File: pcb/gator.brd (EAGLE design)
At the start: 101.6 x 81.3 mm, 81 parts, among them J2 POWER_JACKPTH, X1 USB-A-S, Y1 12MHz

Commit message: any recent changes before break
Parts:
- moved C9 34.9 mm to (90.2, 41.9), turned to 0 degrees
- moved D1 18.5 mm to (76.2, 72.4), turned to 90 degrees
- moved C14 13.3 mm to (96.5, 53.3), turned to 90 degrees
- moved C31 13.0 mm to (86.4, 35.6)
- moved R10 11.7 mm to (82.5, 64.8), turned to 90 degrees
- moved R7 10.9 mm to (90.2, 50.2), turned to 0 degrees
- moved C8 10.8 mm to (81.3, 38.1)
- moved C7 7.73 mm to (86.4, 47.0)
- moved R26 7.67 mm to (59.7, 71.8), turned to 0 degrees
- moved MIC5219-3.3YM5_1 6.35 mm to (90.2, 47.0)
- moved R24 6.35 mm to (71.1, 15.2), turned to 270 degrees
- moved R9 5.08 mm to (87.6, 58.4)
- moved C23 3.81 mm to (77.5, 45.7)
- moved R12 3.81 mm to (81.3, 47.0)
- moved OSC_50M 2.01 mm to (59.1, 67.3), turned to 270 degrees
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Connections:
- net N$10 renamed RD-
- net N$11 renamed TD+
- net N$12 renamed TD-
- net N$9 renamed RD+
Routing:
- net +3V3: track 56.1 -> 126.5 mm, vias 2 -> 3
- net V+: track 0.00 -> 58.7 mm
- net VCCIO: track 206.6 -> 234.4 mm
- net TD-: track 0.00 -> 20.2 mm
- net TD+: track 0.00 -> 19.2 mm
- net RD-: track 0.00 -> 14.6 mm
- net N$3: track 21.0 -> 6.46 mm
- net RD+: track 0.00 -> 12.6 mm
- net NRST: track 45.0 -> 50.2 mm
- net N$7: track 0.00 -> 3.05 mm
- net N$5: track 0.00 -> 1.92 mm
- net SD_DETECT: track 32.2 -> 33.9 mm
- net TDO/SWO: vias 0 -> 1

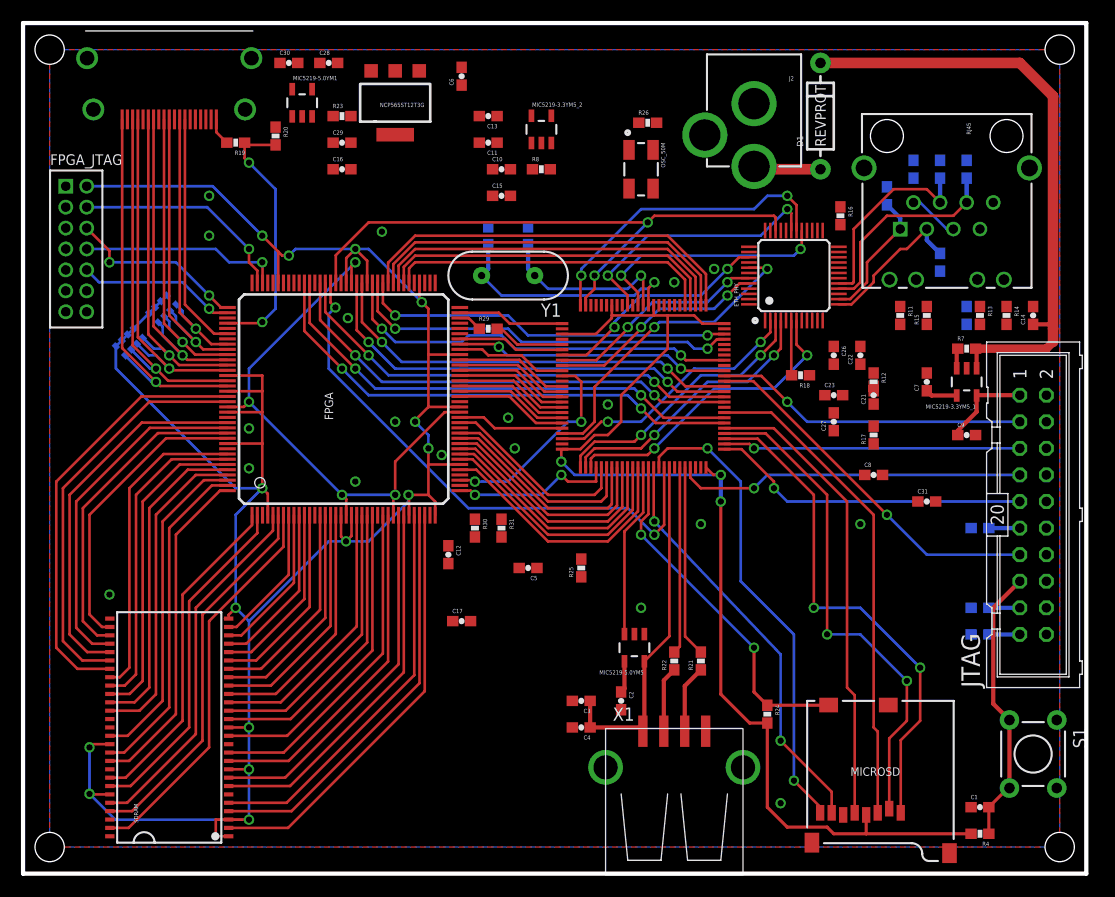
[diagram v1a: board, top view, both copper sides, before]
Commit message: Routed and cleaned up USB power, SD card signals, ethernet phy
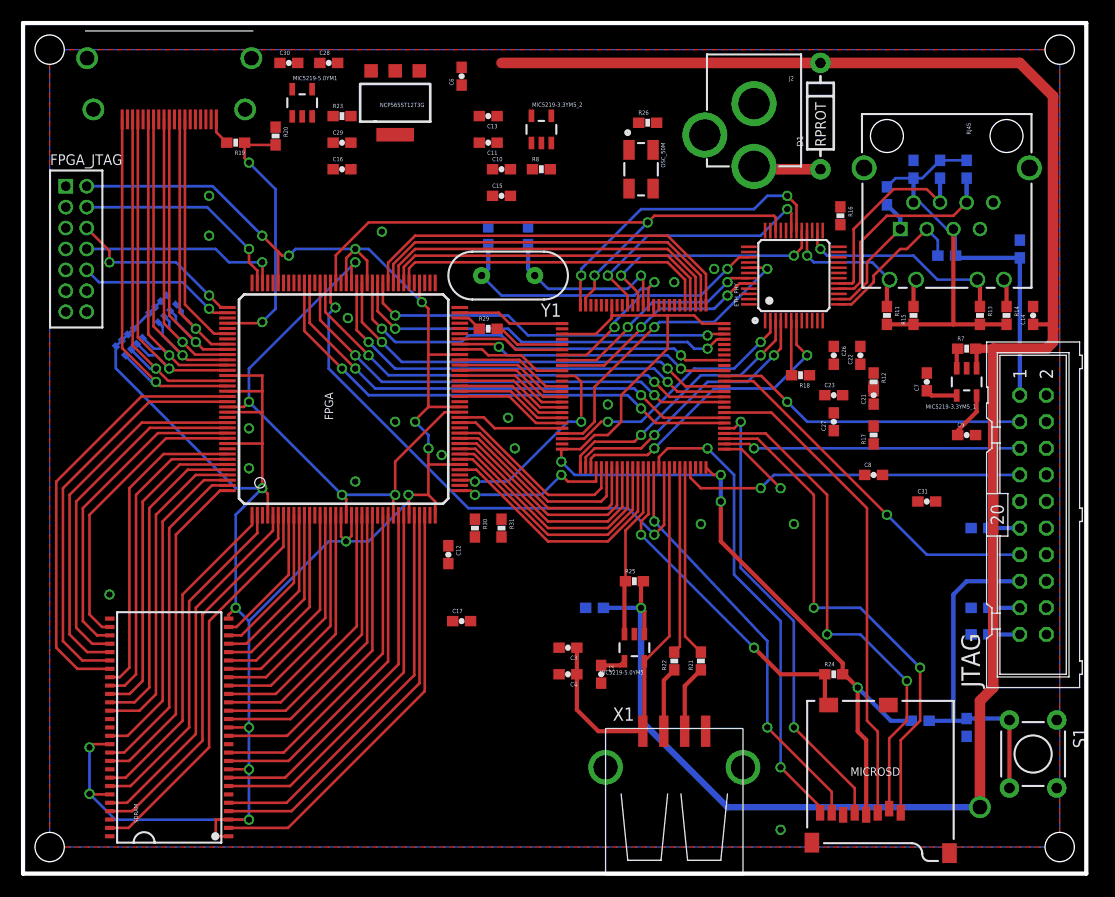
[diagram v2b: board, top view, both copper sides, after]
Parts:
- D1: value REVPROT -> RPROT
- moved R4 12.2 mm to (85.7, 14.6), flipped to the bottom, turned to 0 degrees
- moved C24 8.13 mm to (95.2, 59.7)
- moved C1 7.73 mm to (90.2, 14.0), flipped to the bottom, turned to 90 degrees
- moved C5 7.41 mm to (54.6, 25.4), flipped to the bottom, turned to 0 degrees
- moved R24 7.41 mm to (77.5, 19.1), turned to 0 degrees
- moved C3 5.24 mm to (52.1, 21.6)
- moved C4 5.24 mm to (52.1, 19.1)
- moved R25 5.24 mm to (58.4, 27.9), turned to 0 degrees
- moved C2 3.18 mm to (55.2, 19.1)
- moved R11 1.27 mm to (82.5, 53.3)
- moved R15 1.27 mm to (85.1, 53.3)
- moved R9 0.90 mm to (88.3, 59.1), turned to 180 degrees
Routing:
- net V+: track 58.7 -> 189.0 mm, vias 1 -> 2
- net +3V3: track 126.5 -> 163.8 mm, vias 3 -> 4
- net TCK/SWCLK: track 30.7 -> 6.92 mm
- net LED_ACT: track 0.00 -> 20.8 mm, vias 0 -> 1
- net LED_LINK: track 0.00 -> 13.9 mm, vias 0 -> 1
- net NRST: track 50.2 -> 56.9 mm
- net USB_VBUS: track 34.0 -> 39.3 mm
- net N$14: track 0.00 -> 2.68 mm
- net N$13: track 0.00 -> 2.68 mm
- net SD_CLK: track 44.7 -> 43.7 mm, vias 0 -> 2
- net SD_DETECT: track 33.9 -> 32.9 mm
- net N$4: track 3.06 -> 2.39 mm

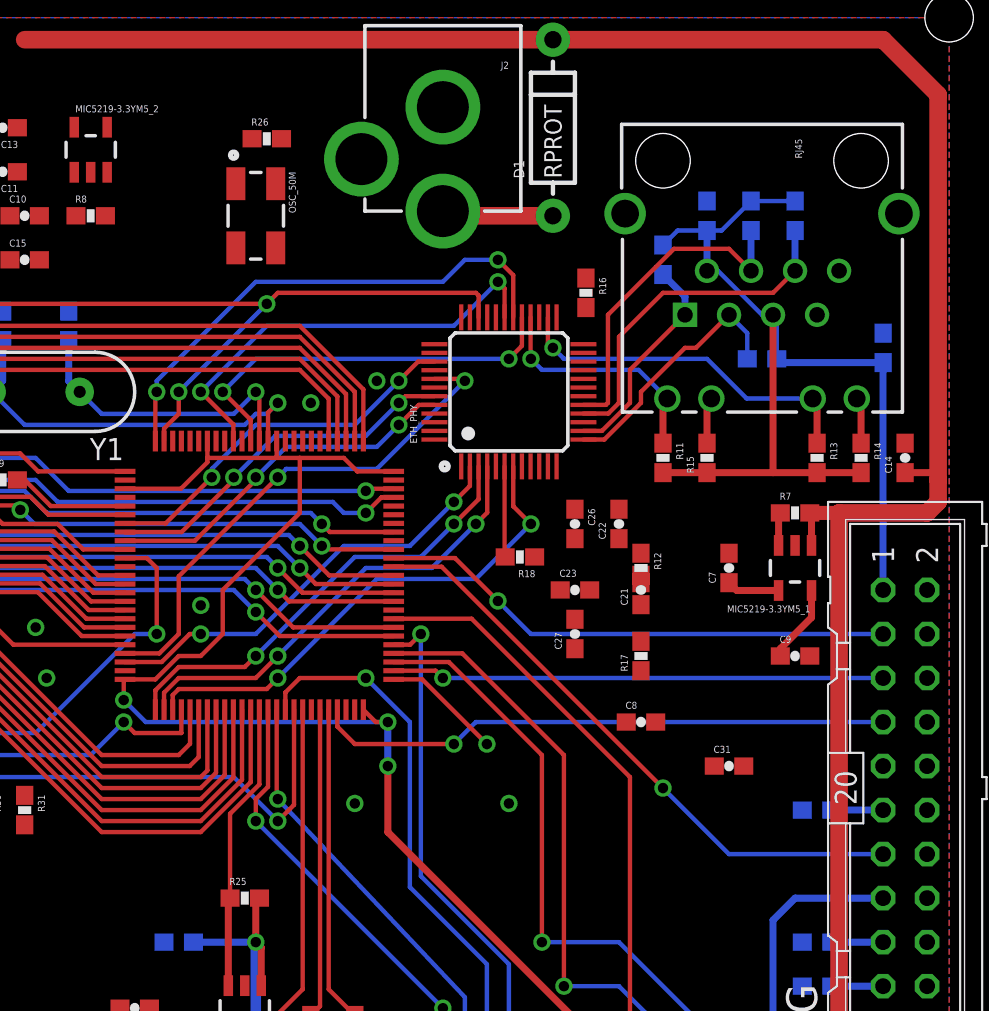
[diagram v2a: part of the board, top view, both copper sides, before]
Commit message: Finished routing ethernet
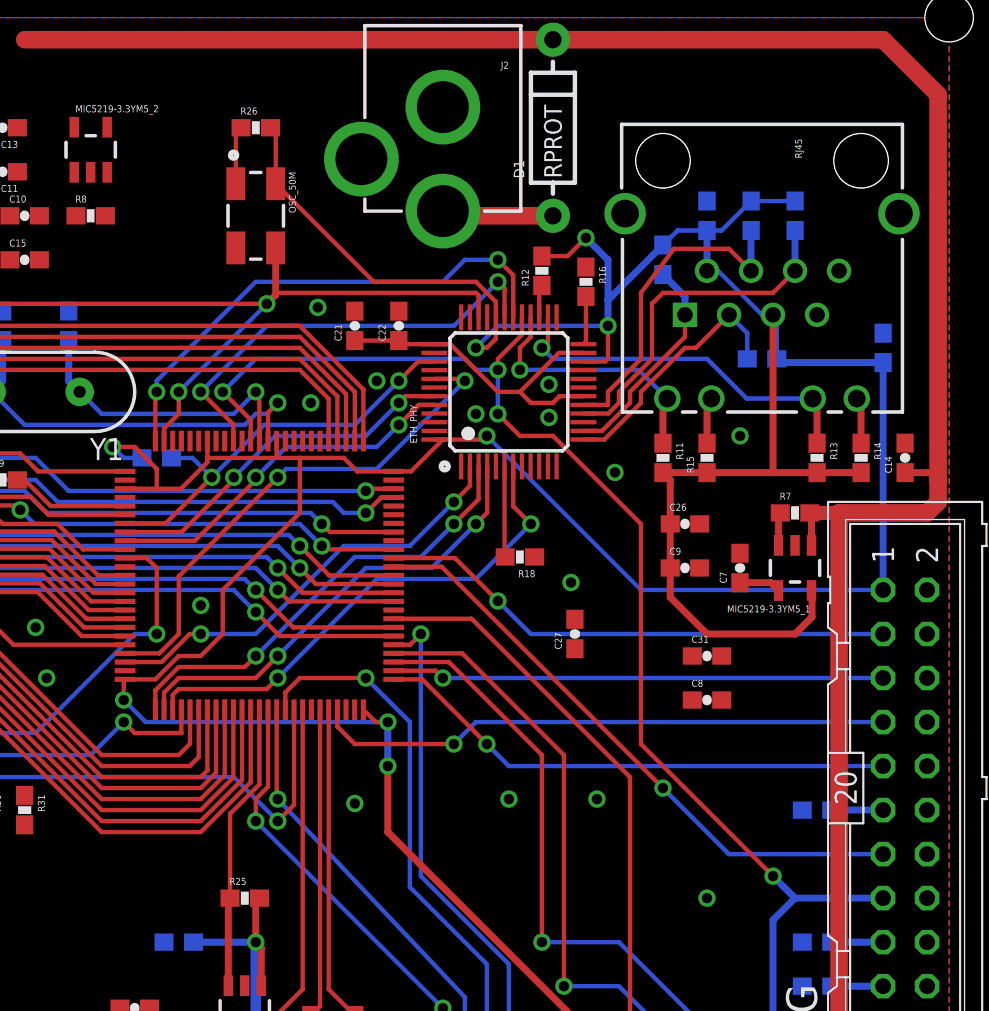
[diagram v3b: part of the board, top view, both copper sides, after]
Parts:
- removed C23: 100n, SparkFun-Passives:0603-CAP
- moved R17 30.2 mm to (53.3, 53.3), flipped to the bottom, turned to 0 degrees
- moved C21 22.5 mm to (64.8, 61.0)
- moved R12 18.1 mm to (75.6, 64.1), turned to 90 degrees
- moved C22 17.1 mm to (67.3, 61.0)
- moved C9 8.13 mm to (83.8, 47.0)
- moved C31 6.48 mm to (85.1, 41.9)
- moved C26 6.35 mm to (83.8, 49.5), turned to 0 degrees
- moved C8 4.02 mm to (85.1, 39.4)
- moved R26 0.90 mm to (59.1, 72.4)
- moved C7 0.64 mm to (87.0, 47.0)
- moved R16 0.63 mm to (78.1, 63.5)
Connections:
- net GND: no longer C23.2
- net PFB: no longer C23.1
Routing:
- net +3V3: track 163.8 -> 264.1 mm, vias 4 -> 9
- net NRST: track 56.9 -> 96.1 mm, vias 2 -> 4
- net TCK/SWCLK: track 6.92 -> 30.3 mm
- net PFB: track 0.00 -> 19.6 mm
- net 50MHZ_OSC: track 57.9 -> 61.4 mm
- net N$31: track 0.00 -> 3.35 mm
- net N$16: track 0.00 -> 2.81 mm
- net RMII_CRSDV: track 22.0 -> 24.5 mm
- net N$17: track 0.00 -> 1.90 mm
- net LED_LINK: track 13.9 -> 15.2 mm
- net LED_ACT: track 20.8 -> 21.4 mm
- net N$7: track 3.05 -> 2.41 mm

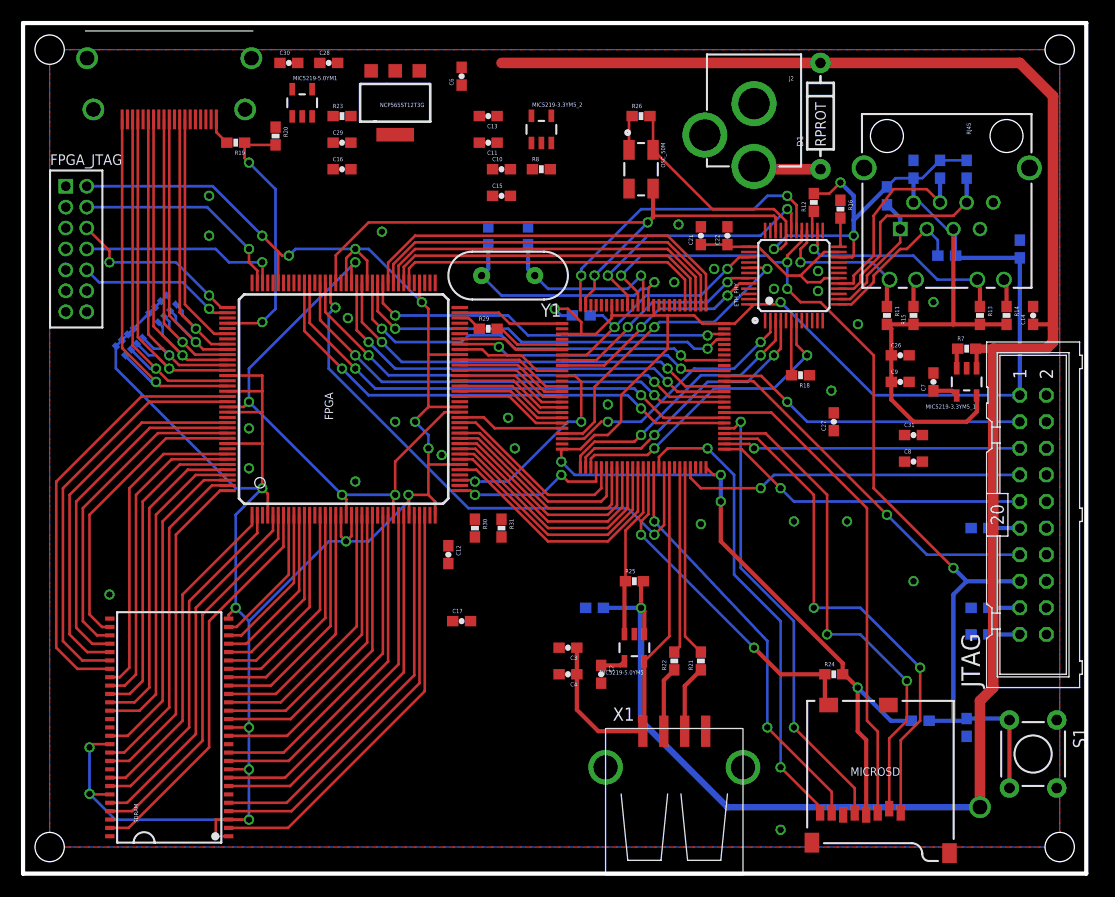
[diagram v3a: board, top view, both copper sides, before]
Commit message: Finished routing CEC, DDC, and remaining power; still have to do decoupling caps
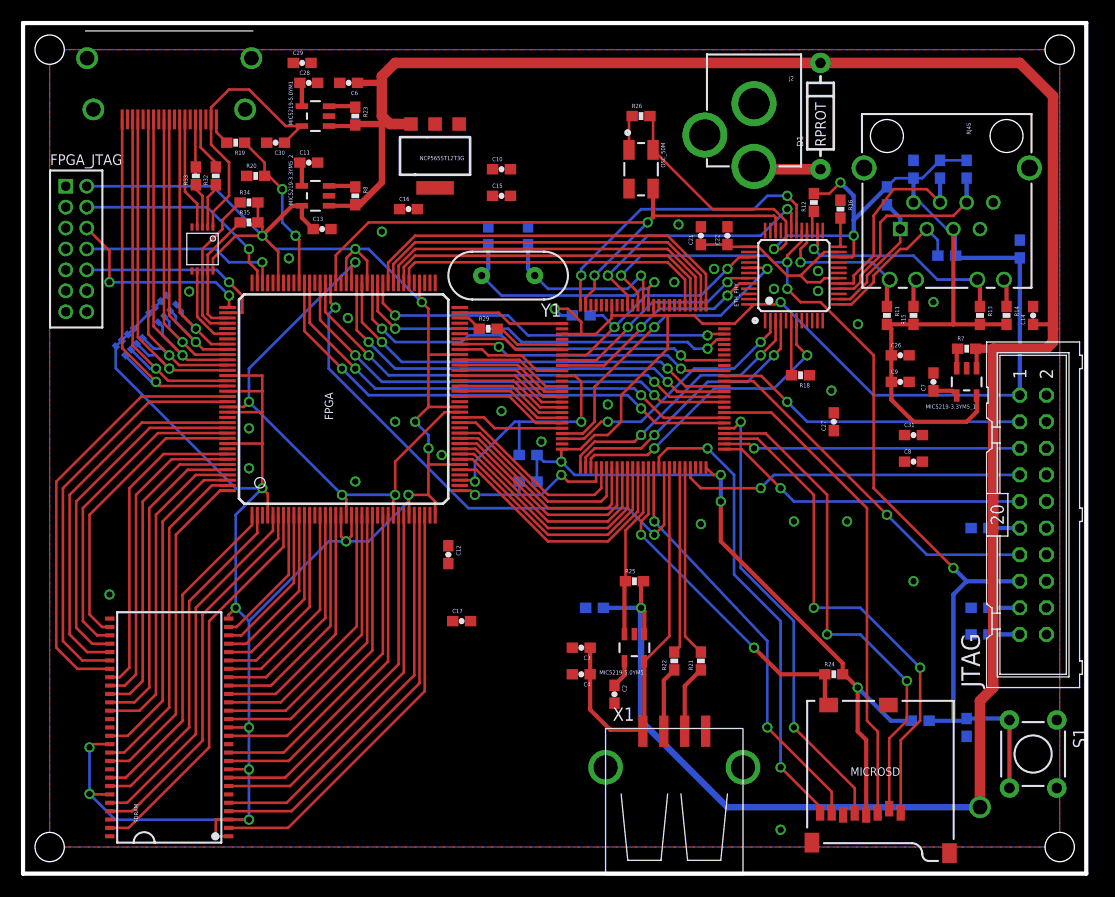
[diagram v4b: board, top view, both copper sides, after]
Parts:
- added R32, R33: 22, SparkFun-Passives:0603-RES
- added R34, R35: 10K, SparkFun-Passives:0603-RES
- added U$3: PCA9527, gator:TSSOP10
- moved MIC5219-3.3YM5_2 22.5 mm to (27.9, 64.8), turned to 90 degrees
- moved C13 19.2 mm to (28.6, 61.6), turned to 0 degrees
- moved R8 18.0 mm to (31.8, 64.8), turned to 270 degrees
- moved C11 17.3 mm to (27.3, 67.9), turned to 0 degrees
- moved C6 10.8 mm to (31.1, 75.6), turned to 180 degrees
- moved C29 8.52 mm to (26.7, 77.5)
- moved C30 7.73 mm to (24.1, 69.8), turned to 180 degrees
- moved R31 7.43 mm to (48.3, 40.0), flipped to the bottom, turned to 180 degrees
- moved C16 7.41 mm to (36.8, 63.5)
- moved R30 6.75 mm to (48.3, 37.5), flipped to the bottom, turned to 180 degrees
- moved NCP565ST12T3G 6.35 mm to (39.4, 68.6)
- moved R20 4.26 mm to (22.2, 66.7), turned to 0 degrees
- moved C28 2.69 mm to (27.3, 75.6)
- moved C2 2.29 mm to (56.5, 17.1)
- moved MIC5219-5.0YM1 1.80 mm to (27.9, 72.4), turned to 90 degrees
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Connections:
- new net CEC_INT: FPGA.P114, U$3.7
- new net DDCC_INT: FPGA.P112, R34.1, U$3.8
- new net DDCD_INT: FPGA.P111, R35.1, U$3.9
- new net DDC_EN: U$3.6
- new net N$10: R33.1, U$3.3
- new net N$9: R32.1, U$3.2
- net CEC: now also U$3.4; no longer FPGA.P114
- net DDC_CLK: now also R33.2
- net DDC_DATA: now also R32.2
- net GND: now also U$3.5
- net HDMI_5V: now also U$3.1
- net HDMI_DETECT: now also FPGA.P99; no longer FPGA.P112
- net VCCIO: now also R34.2, R35.2, U$3.10
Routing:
- net V+: track 189.0 -> 229.5 mm
- net HDMI_5V: track 0.00 -> 25.9 mm
- net VCCIO: track 234.4 -> 253.8 mm, vias 15 -> 14
- net DDCC_INT: track 0.00 -> 15.0 mm
- net CEC: track 22.9 -> 10.8 mm
- net DDCD_INT: track 0.00 -> 12.1 mm
- net HDMI_DETECT: track 25.3 -> 15.8 mm
- net CEC_INT: track 0.00 -> 7.94 mm
- net DDC_CLK: track 0.00 -> 5.74 mm
- net DDC_DATA: track 0.00 -> 5.15 mm
- net +3V3: track 264.1 -> 269.2 mm
- net N$9: track 0.00 -> 4.35 mm
- net N$10: track 0.00 -> 4.30 mm
- net INIT_B: track 19.9 -> 24.2 mm
- net FPGA_TDI: track 15.1 -> 19.0 mm
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
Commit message: More power supply cleanup; 3 airwires remaining
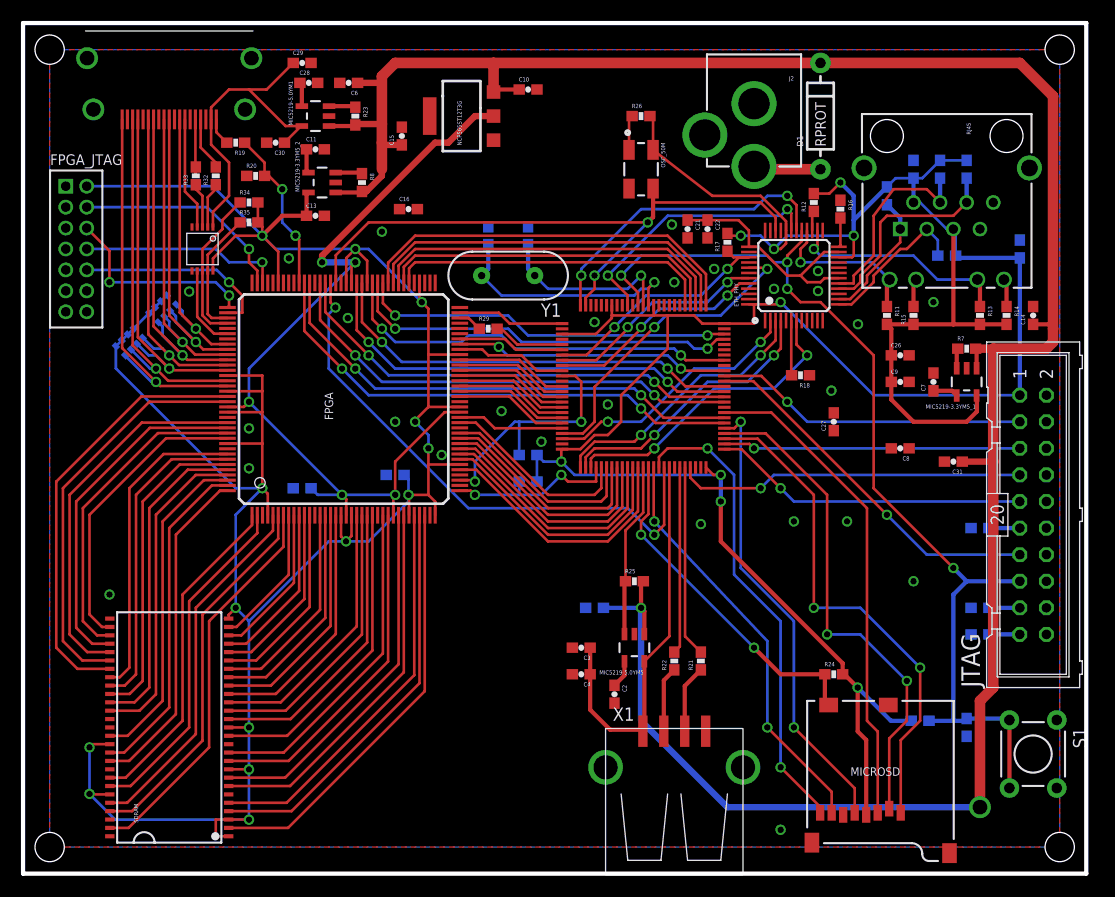
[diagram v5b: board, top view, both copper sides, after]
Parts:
- moved C17 19.8 mm to (26.7, 36.8), flipped to the bottom
- moved R17 15.6 mm to (67.3, 60.3), flipped to the top, turned to 90 degrees
- moved C15 11.1 mm to (36.2, 70.5), turned to 90 degrees
- moved C12 9.16 mm to (35.6, 38.1), flipped to the bottom, turned to 0 degrees
- moved C10 8.03 mm to (48.3, 74.9)
- moved C31 4.58 mm to (88.9, 39.4), turned to 180 degrees
- moved NCP565ST12T3G 4.58 mm to (41.9, 72.4), turned to 90 degrees
- moved C22 2.01 mm to (65.4, 61.6), turned to 270 degrees
- moved C8 1.80 mm to (83.8, 40.6), turned to 180 degrees
- moved C11 1.42 mm to (27.9, 69.2)
- moved MIC5219-3.3YM5_2 1.42 mm to (28.6, 66.0)
- moved R8 1.42 mm to (32.4, 66.0)
- moved C13 1.42 mm to (27.9, 62.9)
- moved C21 1.42 mm to (63.5, 61.6), turned to 270 degrees
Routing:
- net VCCINT: track 55.0 -> 84.0 mm, vias 4 -> 5
- net HDMI_5V: track 25.9 -> 31.2 mm
- net V+: track 229.5 -> 233.9 mm
- net PFB: track 19.6 -> 22.6 mm
- net VCCIO: track 253.8 -> 255.6 mm
